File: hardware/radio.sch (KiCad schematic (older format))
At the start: 8 parts

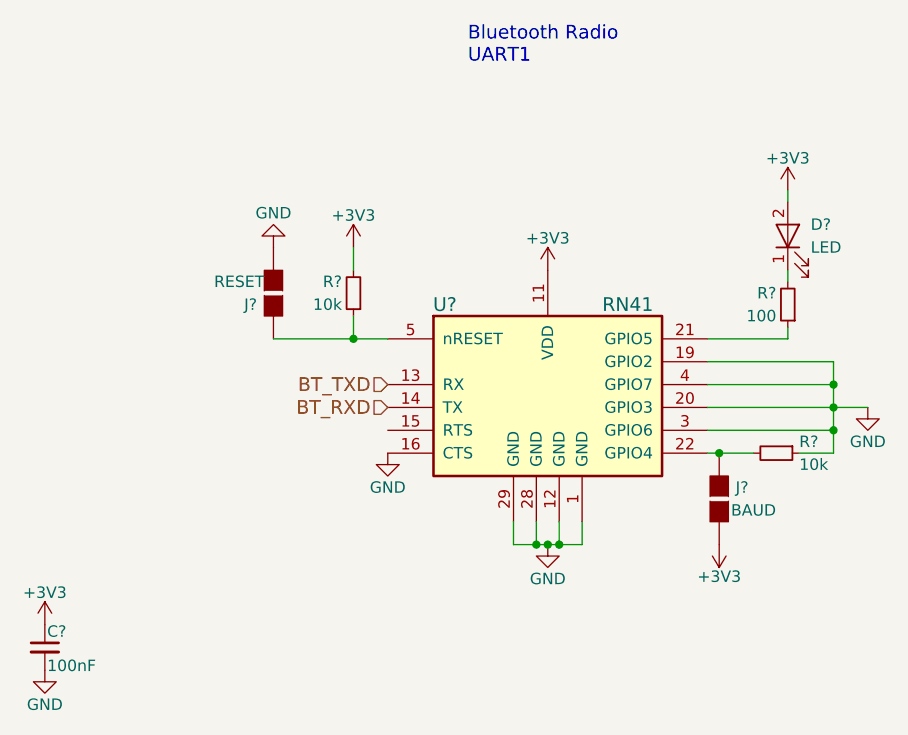
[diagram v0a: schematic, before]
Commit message: Layed board out for the third time. Doesn't include power traces yet.
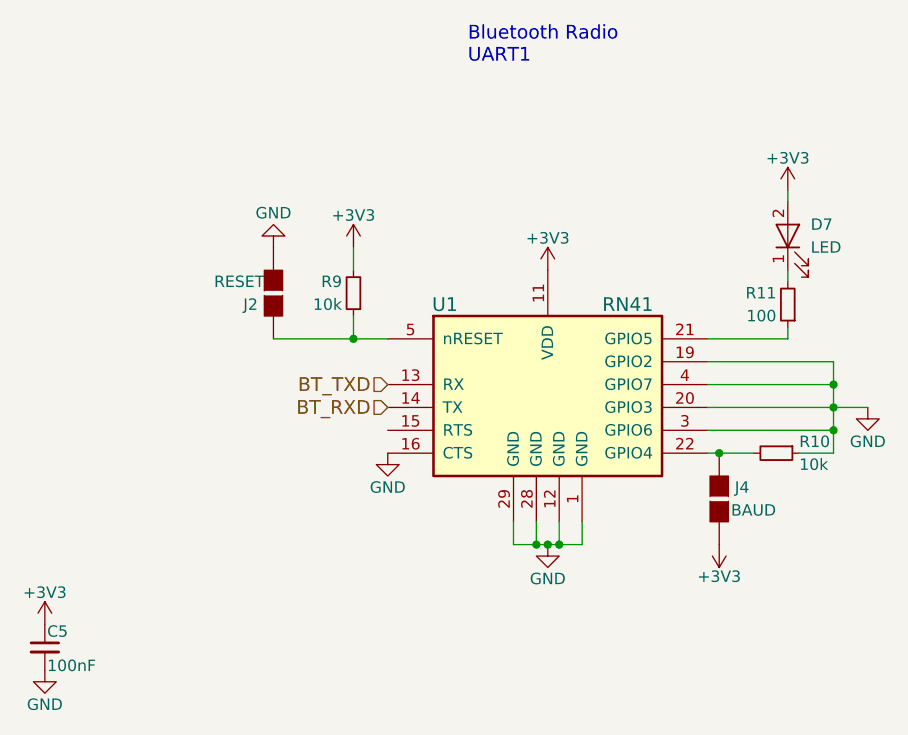
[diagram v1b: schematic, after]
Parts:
- U1: renamed from U?; footprint modules:RN41 -> parts:RN41
- gave numbers to parts that had none: 7
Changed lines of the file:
@@
 EESchema Schematic File Version 2
+LIBS:power
+LIBS:device
+LIBS:transistors
+LIBS:conn
+LIBS:linear
+LIBS:regul
+LIBS:74xx
+LIBS:cmos4000
+LIBS:adc-dac
+LIBS:memory
+LIBS:xilinx
+LIBS:microcontrollers
+LIBS:dsp
+LIBS:microchip
+LIBS:analog_switches
+LIBS:motorola
+LIBS:texas
+LIBS:intel
+LIBS:audio
+LIBS:interface
+LIBS:digital-audio
+LIBS:philips
+LIBS:display
+LIBS:cypress
+LIBS:siliconi
+LIBS:opto
+LIBS:atmel
+LIBS:contrib
+LIBS:valves
+LIBS:stm32
+LIBS:switches
 LIBS:parts
 LIBS:minibot-cache
@@
 $Descr A4 11693 8268
 encoding utf-8
-Sheet 3 5
+Sheet 3 4
 Title ""
 Date ""
@@
 $EndDescr
 $Comp
-L RN41 U?
+L RN41 U1
 U 1 1 59A483B6
 P 5050 3350
-F 0 "U?" H 5100 3400 60  0000 C CNN
+F 0 "U1" H 5100 3400 60  0000 C CNN
 F 1 "RN41" H 5900 3400 60  0000 C CNN
-F 2 "modules:RN41" H 5050 3350 60  0001 C CNN
+F 2 "parts:RN41" H 5050 3350 60  0001 C CNN
 F 3 "" H 5050 3350 60  0001 C CNN
 	1    5050 3350
@@
 $EndComp
 $Comp
-L GND #PWR?
+L GND #PWR035
 U 1 1 59A483BD
 P 6950 3750
-F 0 "#PWR?" H 6950 3500 50  0001 C CNN
+F 0 "#PWR035" H 6950 3500 50  0001 C CNN
 F 1 "GND" H 6950 3600 50  0000 C CNN
 F 2 "" H 6950 3750 50  0001 C CNN
@@
 $EndComp
 $Comp
-L R_Small R?
+L R_Small R10
 U 1 1 59A483C3
 P 6550 3950
-F 0 "R?" V 6500 4050 50  0000 L CNN
+F 0 "R10" V 6500 4050 50  0000 L CNN
 F 1 "10k" V 6600 4050 50  0000 L CNN
 F 2 "Resistors_SMD:R_0603" H 6550 3950 50  0001 C CNN
@@
 $EndComp
 $Comp
-L GS2 J?
+L GS2 J4
 U 1 1 59A483CA
 P 6300 4150
-F 0 "J?" H 6400 4200 50  0000 C CNN
+F 0 "J4" H 6400 4200 50  0000 C CNN
 F 1 "BAUD" H 6450 4100 50  0000 C CNN
 F 2 "Connectors:GS2" V 6374 4150 50  0001 C CNN
@@
 $EndComp
 $Comp
-L LED D?
+L LED D7
 U 1 1 59A483D1
 P 6600 3000
-F 0 "D?" V 6650 2900 50  0000 R CNN
+F 0 "D7" V 6650 2900 50  0000 R CNN
 F 1 "LED" V 6550 2900 50  0000 R CNN
 F 2 "LEDs:LED_0603" H 6600 3000 50  0001 C CNN
@@
 $EndComp
 $Comp
-L R_Small R?
+L R_Small R11
 U 1 1 59A483D8
 P 6600 3300
-F 0 "R?" H 6650 3250 50  0000 L CNN
+F 0 "R11" H 6650 3250 50  0000 L CNN
 F 1 "100" H 6650 3350 50  0000 L CNN
 F 2 "Resistors_SMD:R_0603" H 6600 3300 50  0001 C CNN
@@
 $EndComp
 $Comp
-L GND #PWR?
+L GND #PWR036
 U 1 1 59A483DF
 P 5550 4350
-F 0 "#PWR?" H 5550 4100 50  0001 C CNN
+F 0 "#PWR036" H 5550 4100 50  0001 C CNN
 F 1 "GND" H 5550 4200 50  0000 C CNN
 F 2 "" H 5550 4350 50  0001 C CNN
@@
 $EndComp
 $Comp
-L GS2 J?
+L GS2 J2
 U 1 1 59A483E5
 P 4350 3250
-F 0 "J?" H 4450 3300 50  0000 C CNN
+F 0 "J2" H 4450 3300 50  0000 C CNN
 F 1 "RESET" H 4500 3200 50  0000 C CNN
 F 2 "Connectors:GS2" V 4424 3250 50  0001 C CNN
@@
 $EndComp
 $Comp
-L R_Small R?
+L R_Small R9
 U 1 1 59A483EC
 P 4700 3250
-F 0 "R?" H 4750 3200 50  0000 L CNN
+F 0 "R9" H 4750 3200 50  0000 L CNN
 F 1 "10k" H 4750 3300 50  0000 L CNN
 F 2 "Resistors_SMD:R_0603" H 4700 3250 50  0001 C CNN
@@
 $EndComp
 $Comp
-L GND #PWR?
+L GND #PWR037
 U 1 1 59A483F3
 P 4350 3050
-F 0 "#PWR?" H 4350 2800 50  0001 C CNN
+F 0 "#PWR037" H 4350 2800 50  0001 C CNN
 F 1 "GND" H 4350 2900 50  0000 C CNN
 F 2 "" H 4350 3050 50  0001 C CNN
@@
 	4700 3150 4700 3050
 $Comp
-L C_Small C?
+L C_Small C5
 U 1 1 59A48417
 P 3350 4800
-F 0 "C?" H 3360 4870 50  0000 L CNN
+F 0 "C5" H 3360 4870 50  0000 L CNN
 F 1 "100nF" H 3360 4720 50  0000 L CNN
 F 2 "Capacitors_SMD:C_0603" H 3350 4800 50  0001 C CNN
@@
 $EndComp
 $Comp
-L GND #PWR?
+L GND #PWR038
 U 1 1 59A4841E
 P 3350 4900
-F 0 "#PWR?" H 3350 4650 50  0001 C CNN
+F 0 "#PWR038" H 3350 4650 50  0001 C CNN
 F 1 "GND" H 3350 4750 50  0000 C CNN
 F 2 "" H 3350 4900 50  0001 C CNN
@@
 $EndComp
 $Comp
-L +3V3 #PWR?
+L +3V3 #PWR039
 U 1 1 59A48424
 P 6600 2800
-F 0 "#PWR?" H 6600 2650 50  0001 C CNN
+F 0 "#PWR039" H 6600 2650 50  0001 C CNN
 F 1 "+3V3" H 6600 2940 50  0000 C CNN
 F 2 "" H 6600 2800 50  0001 C CNN
@@
 $EndComp
 $Comp
-L +3V3 #PWR?
+L +3V3 #PWR040
 U 1 1 59A4842A
 P 4700 3050
-F 0 "#PWR?" H 4700 2900 50  0001 C CNN
+F 0 "#PWR040" H 4700 2900 50  0001 C CNN
 F 1 "+3V3" H 4700 3190 50  0000 C CNN
 F 2 "" H 4700 3050 50  0001 C CNN
@@
 $EndComp
 $Comp
-L +3V3 #PWR?
+L +3V3 #PWR041
 U 1 1 59A48430
 P 6300 4350
-F 0 "#PWR?" H 6300 4200 50  0001 C CNN
+F 0 "#PWR041" H 6300 4200 50  0001 C CNN
 F 1 "+3V3" H 6300 4490 50  0000 C CNN
 F 2 "" H 6300 4350 50  0001 C CNN
@@
 $EndComp
 $Comp
-L +3V3 #PWR?
+L +3V3 #PWR042
 U 1 1 59A48436
 P 3350 4700
-F 0 "#PWR?" H 3350 4550 50  0001 C CNN
+F 0 "#PWR042" H 3350 4550 50  0001 C CNN
 F 1 "+3V3" H 3350 4840 50  0000 C CNN
 F 2 "" H 3350 4700 50  0001 C CNN
@@
 $EndComp
 $Comp
-L GND #PWR?
+L GND #PWR043
 U 1 1 59A4843C
 P 4850 3950
-F 0 "#PWR?" H 4850 3700 50  0001 C CNN
+F 0 "#PWR043" H 4850 3700 50  0001 C CNN
 F 1 "GND" H 4850 3800 50  0000 C CNN
 F 2 "" H 4850 3950 50  0001 C CNN
@@
 $EndComp
 $Comp
-L +3V3 #PWR?
+L +3V3 #PWR044
 U 1 1 59A48442
 P 5550 3150
-F 0 "#PWR?" H 5550 3000 50  0001 C CNN
+F 0 "#PWR044" H 5550 3000 50  0001 C CNN
 F 1 "+3V3" H 5550 3290 50  0000 C CNN
 F 2 "" H 5550 3150 50  0001 C CNN
